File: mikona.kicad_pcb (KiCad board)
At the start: 4 copper layers, 50 x 40 mm, 79 parts, among them J1 TC2030-IDC-NL, Q1 BSC109N10NS3G, Q2 STN3N40K3, Q3 IGB50N60T, Q4 IGB50N60T, U1 LT3750EMSTR, U10 MX25V1006FZUI, U11 MIC5528-3.3, U2 ZXGD3009E6, U3 NCS325, U4 STM32F042G6Ux, U5 IX4427MTR, U6 KTD2026EWE-TR, U7 ATA6561-GBQW, U8 AP63205WU, U9 MCP4562T-503E

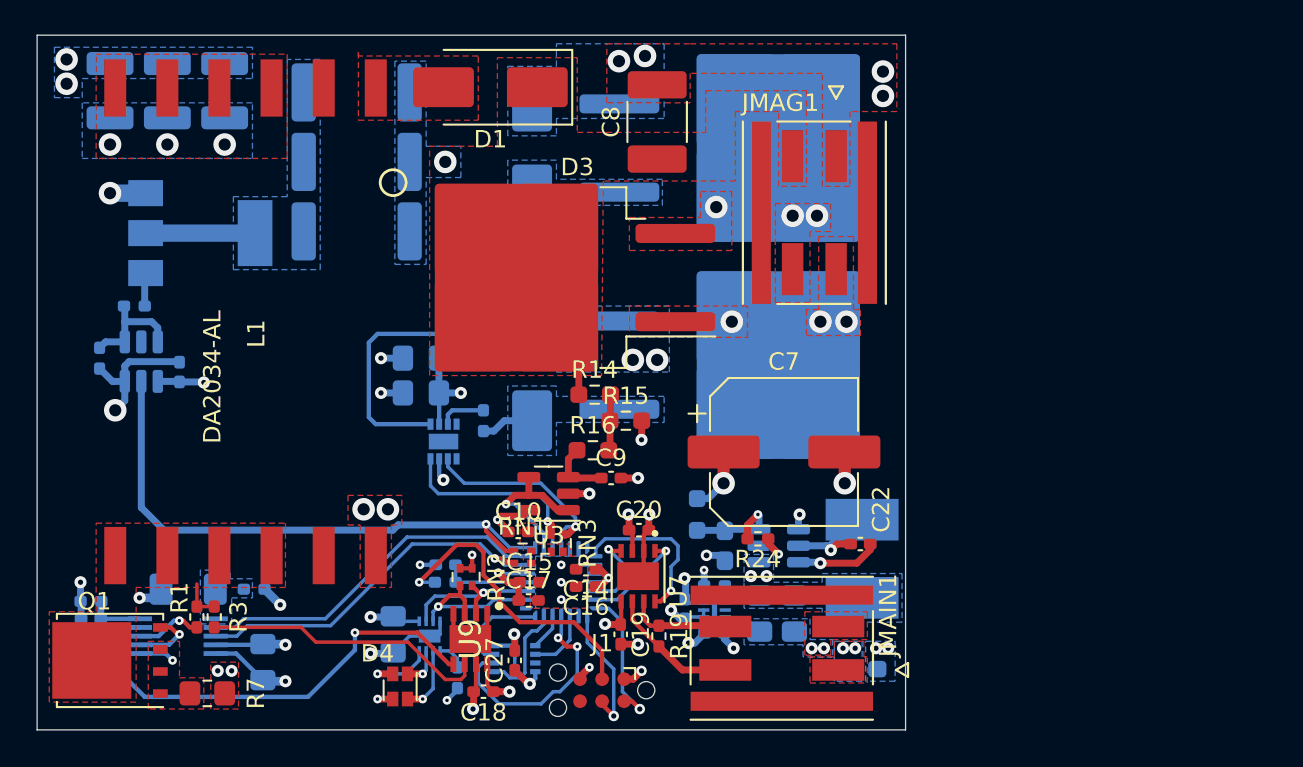
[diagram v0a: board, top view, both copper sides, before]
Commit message: Organize silkscreen and improve power layer.
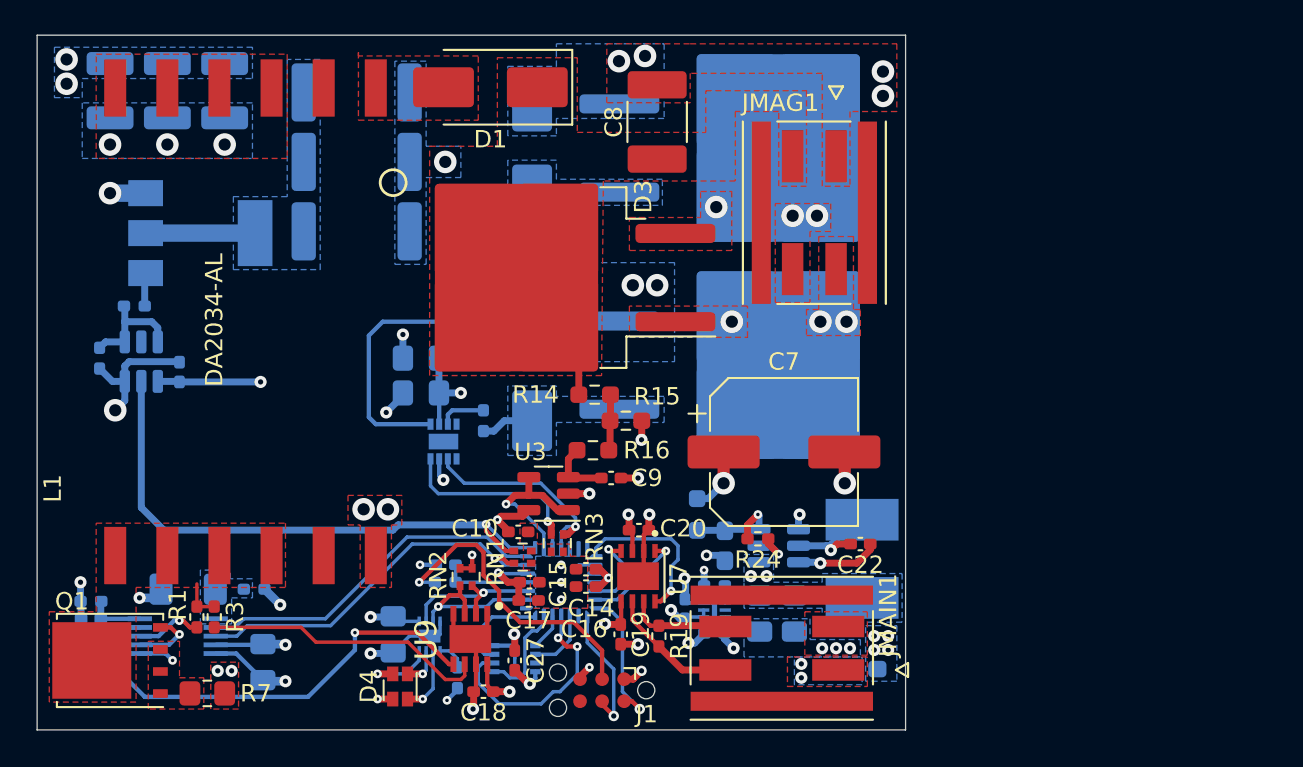
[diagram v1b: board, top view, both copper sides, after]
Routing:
- net +24V: track 17.2 -> 20.5 mm, vias 10 -> 12
- net GND: track 58.3 -> 58.6 mm, vias 40 -> 41
- added copper zone on In2.Cu, net GND
- removed copper zone on In2.Cu, net (none)

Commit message: Improve regulator routing.
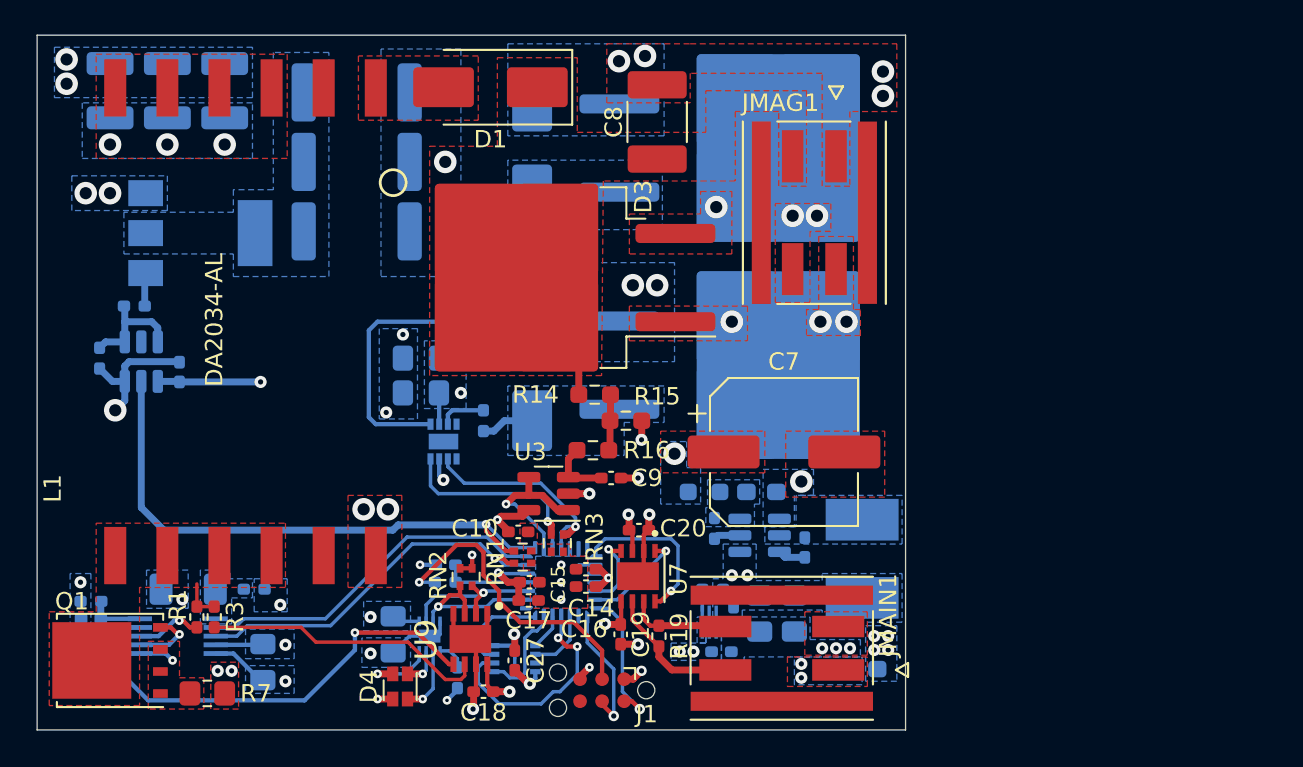
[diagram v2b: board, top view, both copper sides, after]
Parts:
- C22, R24: moved to B.Cu
- moved C24 3.74 mm to (165.2, 111.3), turned to 0 degrees
- moved C29 3.24 mm to (162.9, 120.5), turned to 0 degrees
- moved C22 3.21 mm to (167.7, 114.5), turned to 90 degrees
- moved R24 2.57 mm to (162.5, 113.4), turned to 90 degrees
- moved C25 1.45 mm to (163.6, 118.5), turned to -90 degrees
- moved FB2 1.36 mm to (161.9, 111.3), turned to 0 degrees
- moved U8 1.25 mm to (165.1, 113.8)
- moved U11 0.76 mm to (162.2, 118.8), turned to 90 degrees
- moved R13 0.22 mm to (162.4, 116.9), turned to 180 degrees
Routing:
- net GND: track 58.6 -> 37.8 mm, vias 41 -> 38
- net +24V: track 20.5 -> 11.1 mm
- net Net-(Q2-D-Pad2): track 6.44 -> 0.14 mm
- net Net-(U8-IN): track 6.13 -> 0.00 mm, vias 1 -> 0
- net Net-(U8-SW): track 6.09 -> 0.00 mm, vias 1 -> 0
- net +5V: track 9.90 -> 5.69 mm, vias 8 -> 6
- net Net-(U8-BST): track 4.80 -> 1.59 mm, vias 1 -> 0
- net +3.3V: track 22.9 -> 20.4 mm, vias 9 -> 10
- net Net-(U8-EN): track 2.47 -> 1.54 mm, vias 1 -> 0
- net /Logic/CAN_RX: track 5.10 -> 4.53 mm
- added copper zone on B.Cu, net +3.3V
- added copper zone on B.Cu, net Net-(U8-IN)
- added copper zone on B.Cu, net Net-(U8-SW)

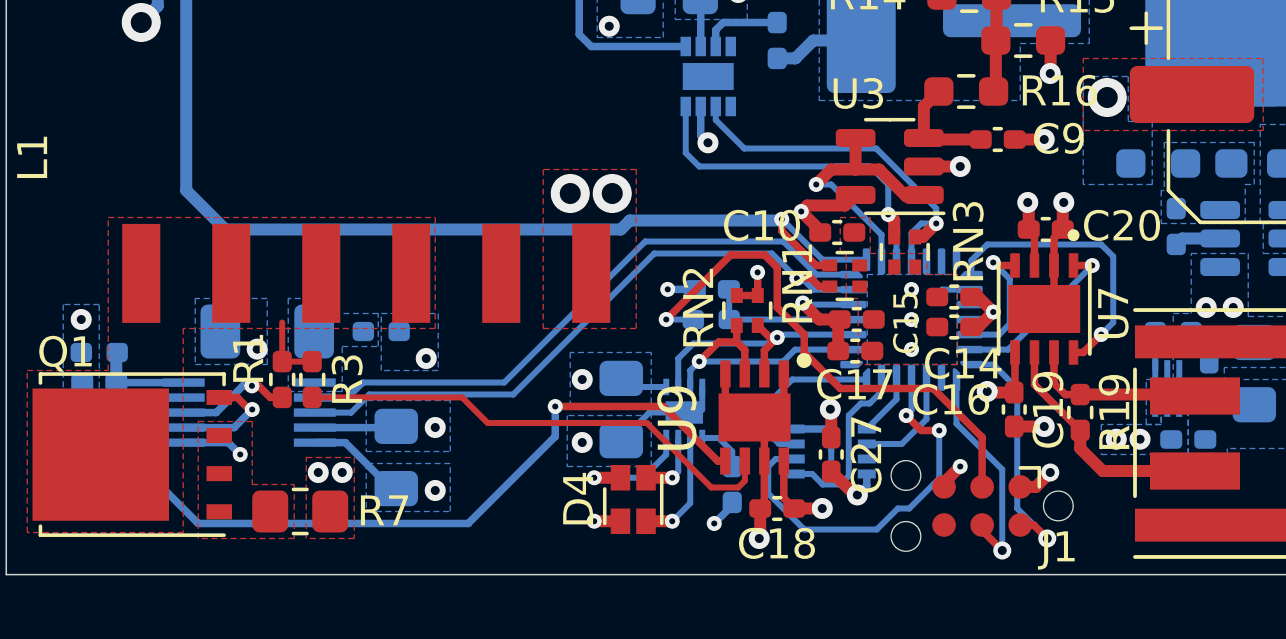
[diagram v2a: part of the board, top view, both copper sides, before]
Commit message: Fix minimum via hole size violations.
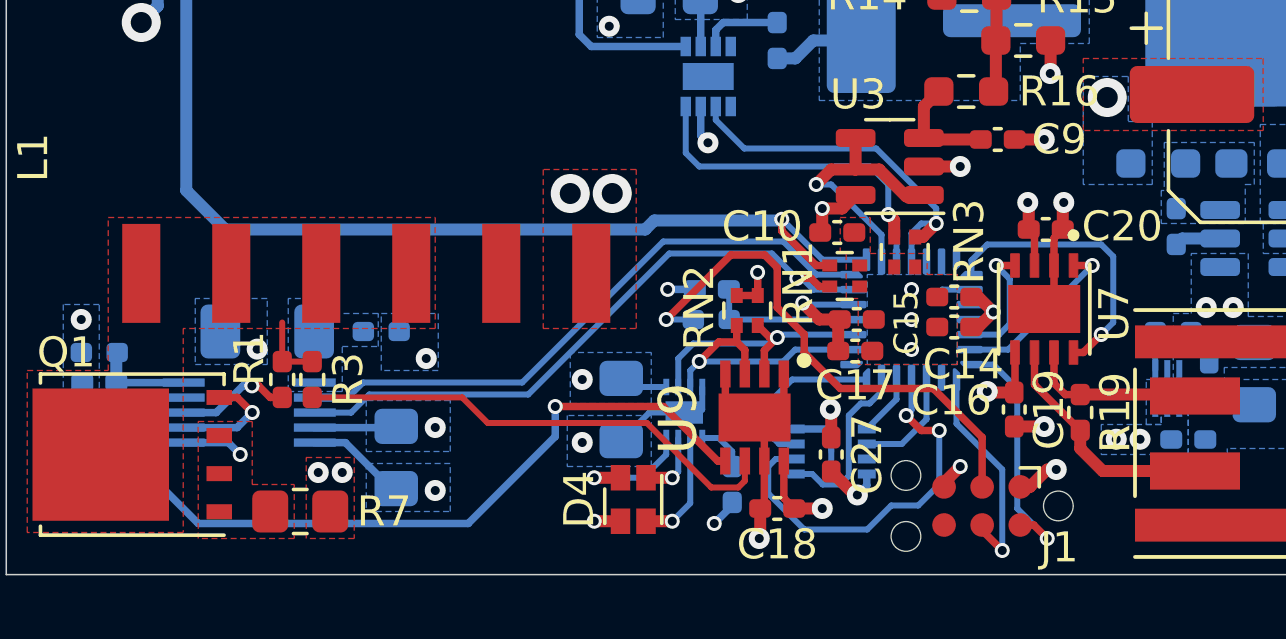
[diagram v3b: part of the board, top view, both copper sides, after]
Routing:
- net +3.3V: track 20.4 -> 19.7 mm

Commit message: Update MPNs and add jlcpcb comments.
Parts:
- Q3, Q4: value IGB50N60T -> IGB50N65S
- R7: value 0.008 -> 0.01
- U7: value ATA6561-GBQW -> ATA6561-GBQW-N

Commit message: Add teardrops and version text.
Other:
- board text added: "V.2023.0.3"

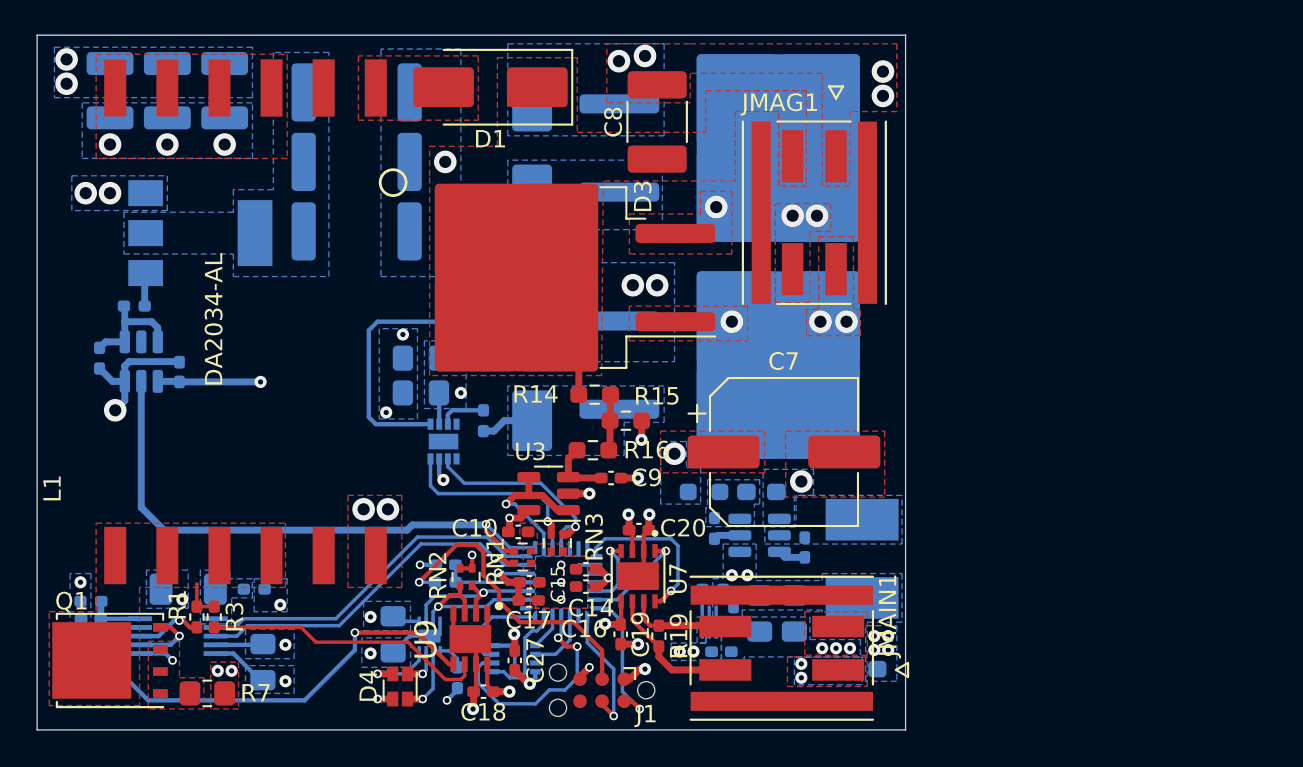
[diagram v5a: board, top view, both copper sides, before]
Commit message: Move from stm32 to pic16 and remove other unnecessary parts.
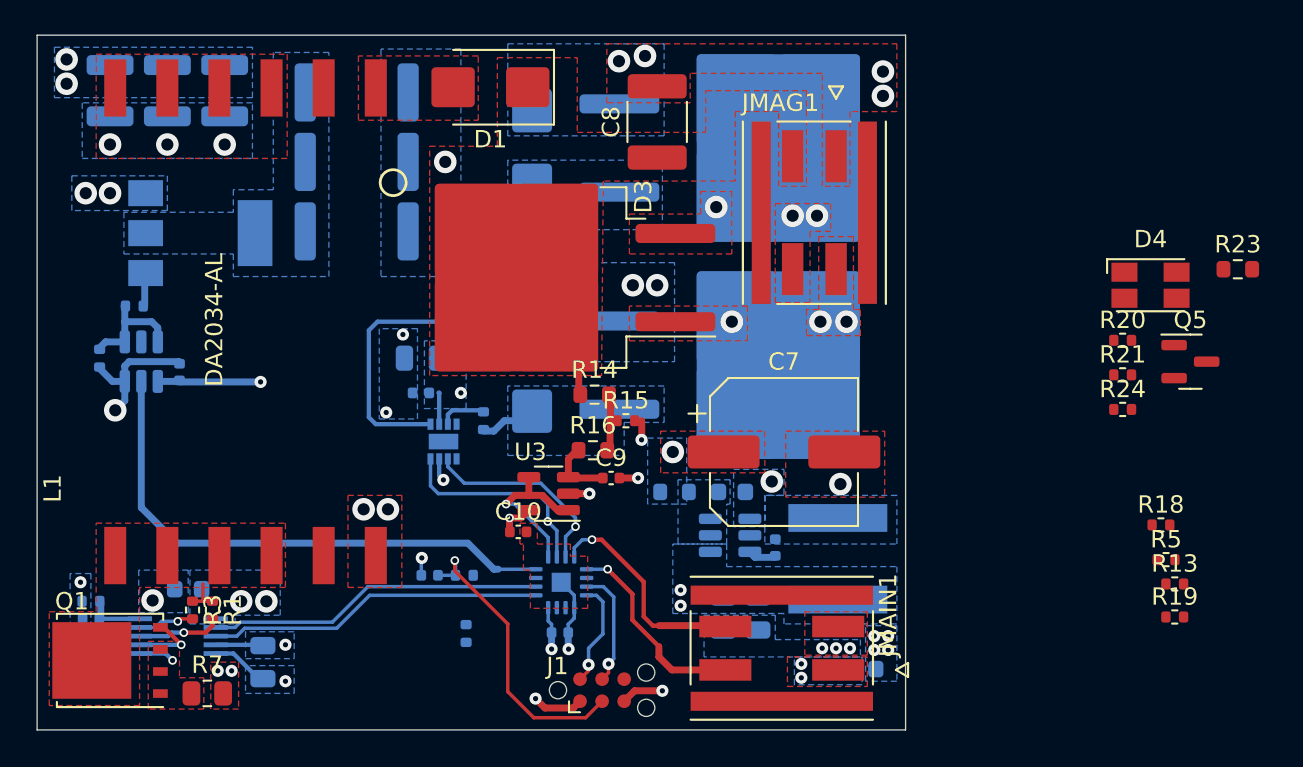
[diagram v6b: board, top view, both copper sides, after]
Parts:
- removed C12: 10µF, Capacitor_SMD:C_0805_2012Metric_Pad1.18x1.45mm_HandSolder
- removed C15, C16, C18, C19, C20, C27: 100nF, Capacitor_SMD:C_0402_1005Metric_Pad0.74x0.62mm_HandSolder
- removed C17: 10uF, Capacitor_SMD:C_0402_1005Metric_Pad0.74x0.62mm_HandSolder
- removed C25, C29: 2.2uF, Capacitor_SMD:C_0402_1005Metric_Pad0.74x0.62mm_HandSolder
- removed RN1, RN3: 100K, Resistor_SMD:R_Array_Convex_2x0402
- removed RN2: 4.7K, Resistor_SMD:R_Array_Convex_2x0402
- removed U10: MX25V1006FZUI, MX25V1006FZUI:PSON50P200X300X60-9N
- removed U11: MIC5528-3.3, MIC5528-3.3YMT-TR:SON40P120X120X60-7N
- removed U6: KTD2026EWE-TR, KTD2026EWE-TR:SON40P150X150X55-9N
- removed U7: ATA6561-GBQW-N, ATA6561-GBQW:SON65P300X300X100-9N
- removed U9: MCP4562T-503E, MCP4562T-503E_MF:SON65P300X300X100-9N-D
- added Q5: BSS138, Package_TO_SOT_SMD:SOT-23, F.Cu at (189.9, 103.8)
- added R18: 100K, Resistor_SMD:R_0402_1005Metric, F.Cu at (188.2, 113.2)
- added R20: 220, Resistor_SMD:R_0402_1005Metric, F.Cu at (186.0, 102.6)
- added R21: 220, Resistor_SMD:R_0402_1005Metric, F.Cu at (186.0, 104.6)
- added R23: 0, Resistor_SMD:R_0603_1608Metric, F.Cu at (192.6, 98.5)
- C1, C13, C26, C28: footprint Capacitor_SMD:C_0805_2012Metric_Pad1.18x1.45mm_HandSolder -> Capacitor_SMD:C_0805_2012Metric
- C10, C22, C23, C3, C9: footprint Capacitor_SMD:C_0402_1005Metric_Pad0.74x0.62mm_HandSolder -> Capacitor_SMD:C_0402_1005Metric
- C11: value 100nF -> 10nF; footprint Capacitor_SMD:C_0402_1005Metric_Pad0.74x0.62mm_HandSolder -> Capacitor_SMD:C_0402_1005Metric
- C14: footprint Capacitor_SMD:C_0402_1005Metric_Pad0.74x0.62mm_HandSolder -> Capacitor_SMD:C_0402_1005Metric; moved to B.Cu
- C2: footprint Capacitor_SMD:C_1206_3216Metric_Pad1.33x1.80mm_HandSolder -> Capacitor_SMD:C_0603_1608Metric
- C21: footprint Capacitor_SMD:C_0805_2012Metric_Pad1.18x1.45mm_HandSolder -> Capacitor_SMD:C_0402_1005Metric
- C24: footprint Capacitor_SMD:C_0603_1608Metric_Pad1.08x0.95mm_HandSolder -> Capacitor_SMD:C_0603_1608Metric
- C4, C5, C6: footprint Capacitor_SMD:C_1210_3225Metric_Pad1.33x2.70mm_HandSolder -> Capacitor_SMD:C_1210_3225Metric
- C8: footprint Capacitor_SMD:C_1812_4532Metric_Pad1.57x3.40mm_HandSolder -> Capacitor_SMD:C_1812_4532Metric
- D1, D2, D5: footprint Diode_SMD:D_SMB_Handsoldering -> Diode_SMD:D_SMB
- D4: value RGB -> LED Dual; footprint LTST-C19HE1WT:LED_LiteOn_LTST-C19HE1WT -> LED_SMD:LED_Avago_PLCC4_3.2x2.8mm_CW
- F1: footprint Fuse:Fuse_0603_1608Metric_Pad1.05x0.95mm_HandSolder -> Fuse:Fuse_0603_1608Metric
- FB2, R14, R16: footprint Resistor_SMD:R_0603_1608Metric_Pad0.98x0.95mm_HandSolder -> Resistor_SMD:R_0603_1608Metric
- L2: value 4.7uH -> 3.9uH; footprint Inductor_SMD:L_Taiyo-Yuden_NR-50xx_HandSoldering -> Inductor_SMD:L_Bourns-SRN6028
- R1, R12, R17, R4, R6, R8: footprint Resistor_SMD:R_0402_1005Metric_Pad0.72x0.64mm_HandSolder -> Resistor_SMD:R_0402_1005Metric
- R10, R11, R9: footprint Resistor_SMD:R_2512_6332Metric_Pad1.40x3.35mm_HandSolder -> Resistor_SMD:R_2512_6332Metric
- R13, R5: value 0 -> 100K; footprint Resistor_SMD:R_0402_1005Metric_Pad0.72x0.64mm_HandSolder -> Resistor_SMD:R_0402_1005Metric; moved to F.Cu
- R15: footprint Resistor_SMD:R_0603_1608Metric_Pad0.98x0.95mm_HandSolder -> Resistor_SMD:R_0402_1005Metric
- R19: value 120 -> 100K; footprint Resistor_SMD:R_0402_1005Metric_Pad0.72x0.64mm_HandSolder -> Resistor_SMD:R_0402_1005Metric
- R2: value 100K -> 10K; footprint Resistor_SMD:R_0402_1005Metric_Pad0.72x0.64mm_HandSolder -> Resistor_SMD:R_0402_1005Metric
- R22: value 0 -> 100; footprint Resistor_SMD:R_0402_1005Metric_Pad0.72x0.64mm_HandSolder -> Resistor_SMD:R_0402_1005Metric
- R24: value 0 -> 10K; footprint Resistor_SMD:R_0402_1005Metric_Pad0.72x0.64mm_HandSolder -> Resistor_SMD:R_0402_1005Metric; moved to F.Cu
- R3: value 10K -> 40.2K; footprint Resistor_SMD:R_0402_1005Metric_Pad0.72x0.64mm_HandSolder -> Resistor_SMD:R_0402_1005Metric
- R7: footprint Resistor_SMD:R_0805_2012Metric_Pad1.20x1.40mm_HandSolder -> Resistor_SMD:R_0805_2012Metric
- U4: value STM32F042G6Ux -> PIC16F15224; footprint Package_DFN_QFN:QFN-28_4x4mm_P0.5mm -> Package_DFN_QFN:VQFN-16-1EP_3x3mm_P0.5mm_EP1.1x1.1mm
- U8: value AP63205WU -> AP63203WU
- moved R5 52.5 mm to (188.5, 115.2), turned to 0 degrees
- moved D4 49.0 mm to (187.6, 99.4)
- moved R19 29.7 mm to (189.0, 118.5), turned to 0 degrees
- moved R13 26.6 mm to (189.0, 116.6), turned to 0 degrees
- moved R24 24.5 mm to (186.0, 106.5), turned to 0 degrees
- moved C14 3.95 mm to (153.6, 119.4), turned to 0 degrees
- moved R2 2.60 mm to (148.2, 119.5)
- moved C26 2.10 mm to (163.0, 118.3)
- moved C28 2.10 mm to (165.0, 118.3)
- moved FB2 1.70 mm to (160.2, 111.3)
- moved C22 1.70 mm to (166.0, 114.5)
- moved C24 1.70 mm to (163.5, 111.3)
- moved U8 1.70 mm to (163.4, 113.8)
- moved L2 1.40 mm to (169.6, 115.2)
- moved R3 1.31 mm to (132.4, 118.1)
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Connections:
- C11 pad 1: Net-(U4-NRST) -> GND
- C11 pad 2: GND -> /Logic/SW_NRST
- C2 pad 2: Net-(U1-VTRANS) -> +24V
- C24 pad 1: Net-(U8-IN) -> Net-(U8-EN)
- C26 pad 1: +5V -> +3.3V
- C28 pad 1: +5V -> +3.3V
- D4 pad 1: Net-(D4-RK) -> Net-(D4-A1)
- D4 pad 3: Net-(D4-BK) -> GND
- D4 pad 4: +5V -> Net-(D4-A1)
- FB2 pad 2: Net-(U8-IN) -> Net-(U8-EN)
- JMAIN1 pad 3: /CAN_N -> /SCL
- JMAIN1 pad 4: /CAN_P -> /SDA
- L2 pad 2: +5V -> +3.3V
- R13 pad 1: +5V -> GND
- R13 pad 2: Net-(U11-EN) -> /Logic/KICK_B
- R19 pad 1: /CAN_P -> GND
- R19 pad 2: /CAN_N -> /Logic/CHARGE
- R2 pad 1: +5V -> /Logic/SW_NRST
- R2 pad 2: Net-(U6-ST) -> +3.3V
- R22 pad 1: Net-(U4-NRST) -> Net-(U4-RA3/~{MCLR}/VPP)
- R24 pad 1: Net-(U8-EN) -> GND
- R24 pad 2: Net-(U8-IN) -> Net-(Q5-G)
- R3 pad 2: Net-(U9-P0B) -> Net-(U1-RVOUT)
- R5 pad 1: +24V -> GND
- R5 pad 2: Net-(U1-VTRANS) -> /Logic/KICK_A
- U1 pad 1: Net-(U1-VTRANS) -> +24V
- U1 pad 9: /Power/RVOUT -> Net-(U1-RVOUT)
- U4 pad 1: unconnected-(U4-PB8-Pad1) -> /Logic/CHARGE
- U4 pad 10: /Logic/KICK_B -> /Logic/LED
- U4 pad 11: /Logic/KICK_A -> /Logic/SWCLK
- U4 pad 12: unconnected-(U4-PA6-Pad12) -> /Logic/SWDIO
- U4 pad 13: unconnected-(U4-PA7-Pad13) -> GND
- U4 pad 15: /Logic/CAN_STB -> unconnected-(U4-NC-Pad15)
- U4 pad 16: GND -> +3.3V
- U4 pad 17: +3.3V -> GND
- U4 pad 2: /Logic/SDA -> /Logic/DONE
- U4 pad 3: /Logic/SCL -> Net-(U4-RA3/~{MCLR}/VPP)
- U4 pad 4: Net-(U4-NRST) -> /Logic/DISCHARGE
- U4 pad 5: +3.3V -> /Logic/VOUT_ADC
- U4 pad 6: /Logic/CHARGE -> /Logic/KICK_B
- U4 pad 7: /Logic/DONE -> /Logic/KICK_A
- U4 pad 8: /Logic/DISCHARGE -> /SDA
- U4 pad 9: /Logic/VOUT_ADC -> /SCL
- U8 pad 1: +5V -> +3.3V
- U8 pad 3: Net-(U8-IN) -> Net-(U8-EN)
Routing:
- net /Power/RVOUT: track 26.8 -> 0.00 mm, vias 1 -> 0
- net Net-(U9-P0B): track 16.4 -> 0.00 mm
- net /Logic/MISO: track 13.2 -> 0.00 mm, vias 2 -> 0
- net /SDA: track 0.00 -> 12.7 mm, vias 0 -> 1
- net GND: track 37.8 -> 25.3 mm, vias 38 -> 32
- net +3.3V: track 19.7 -> 7.54 mm, vias 10 -> 5
- net /SCL: track 0.00 -> 11.6 mm, vias 0 -> 1
- net /Logic/CAN_STB: track 9.53 -> 0.00 mm, vias 1 -> 0
- net /Logic/SDA: track 9.53 -> 0.00 mm, vias 1 -> 0
- net /Logic/SCL: track 9.33 -> 0.00 mm, vias 1 -> 0
- net /CAN_N: track 7.97 -> 0.00 mm
- net /Logic/FLASH_CS: track 5.93 -> 0.00 mm
- net /CAN_P: track 5.90 -> 0.00 mm
- net /Logic/CAN_TX: track 5.87 -> 0.00 mm, vias 1 -> 0
- net +5V: track 5.69 -> 0.00 mm, vias 6 -> 0
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- added copper zone on B.Cu, net Net-(U8-EN)
- removed copper zone on B.Cu, net +5V
- removed copper zone on In2.Cu, net +5V
- removed copper zone on B.Cu, net Net-(U1-VTRANS)
- removed copper zone on B.Cu, net Net-(U8-IN)
